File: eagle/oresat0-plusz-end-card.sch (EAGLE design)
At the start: 36 parts, among them J1 Harwin M55-7101242R, J10 R107064070_CONTACT, J11 R107064070_CONTACT, J12 R107064070_CONTACT, J13 R107064070_CONTACT, J14 R107064070_CONTACT, J15 R107064070_CONTACT, J16 R107064070_CONTACT, J2 Harwin M55-7101242R, J3 Harwin M55-7101242R, J4 Harwin M55-7101242R, J6 J-SAMTEC-TFM-120-X1-XXX-D-RA, J7 R107064070_CONTACT, J8 R107064070_CONTACT, J9 R107064070_CONTACT, U1 QCN-19D+, U2 QCN-19D+, U3 QCN-19D+

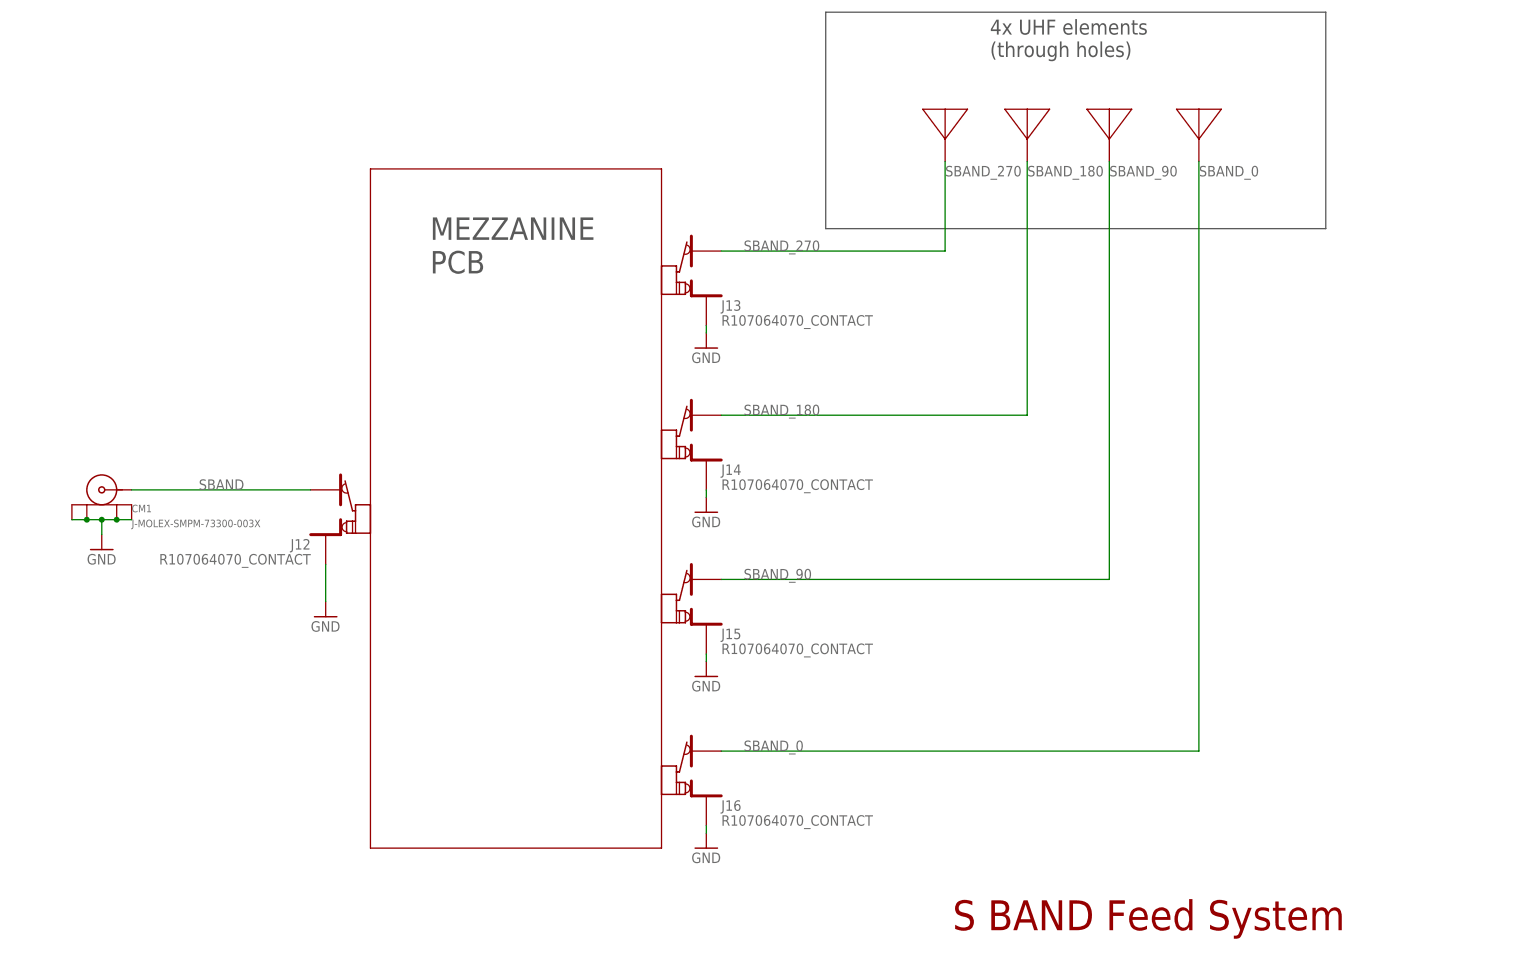
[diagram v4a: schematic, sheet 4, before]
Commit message: Version 1.2 of the OreSat0 end card and mezzanine.
Largest change is the position of the antennas on the end card; changes to the deployer changed the antenna placement which triggered everything else.

Other changes include fiducials, attributes cleanup, move to 0603 resistors, and misc polish.
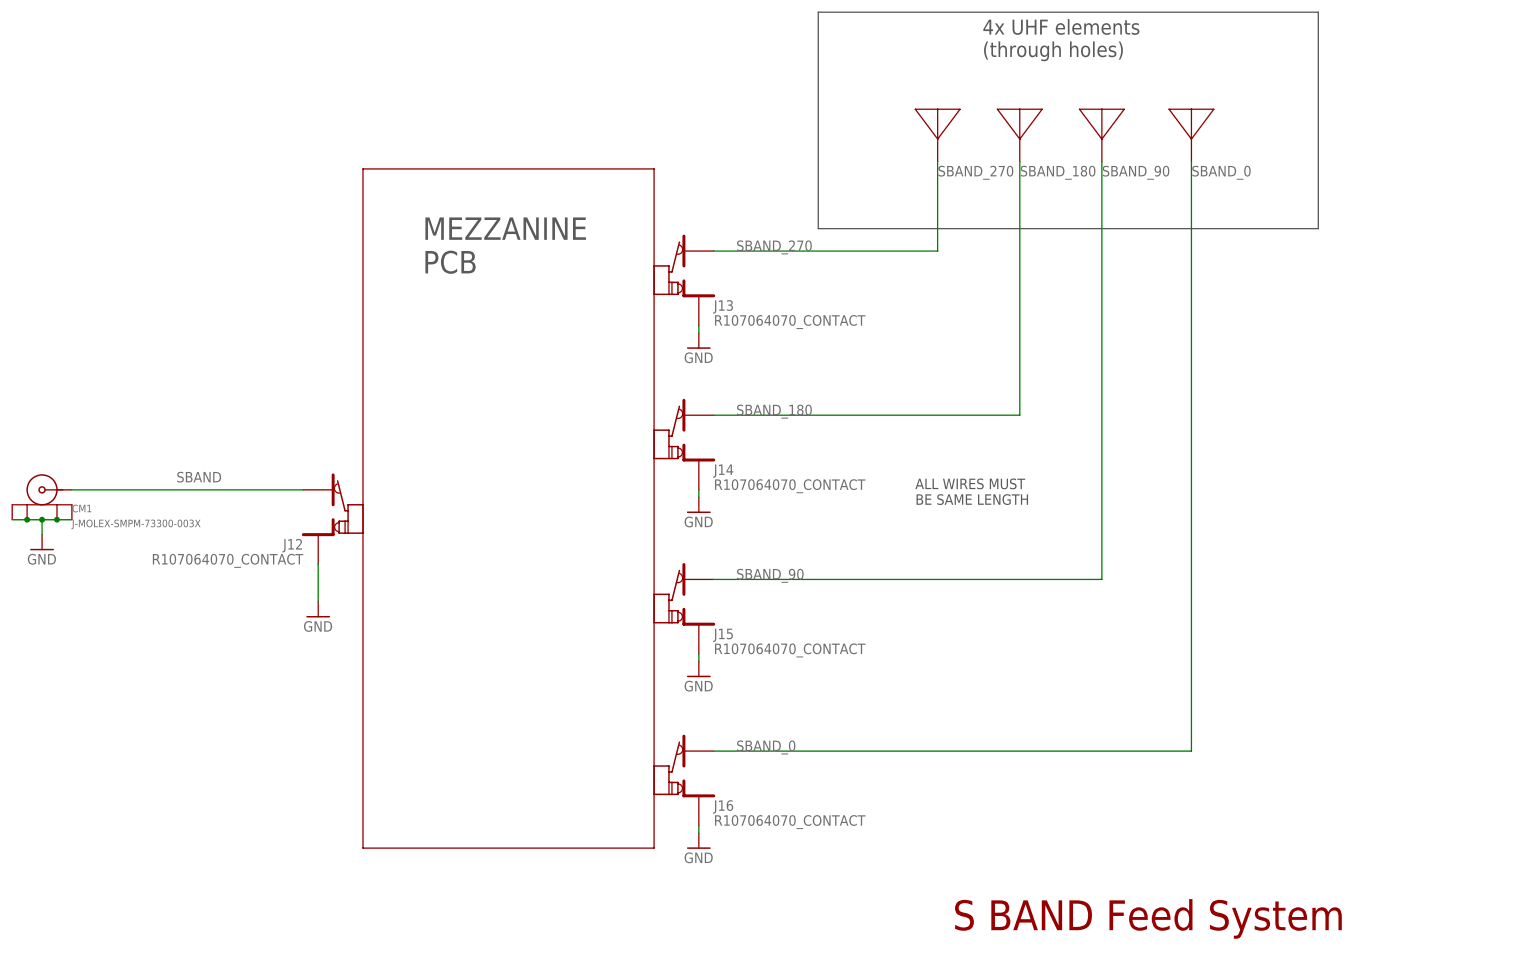
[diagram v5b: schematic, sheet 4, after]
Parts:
- added FIDUCIAL1, FIDUCIAL2, FIDUCIAL3, FIDUCIAL4, FIDUCIAL5, FIDUCIAL6: FIDUCIAL-1.0X2.0, monitor-v2-debug:FIDUCIAL-1.0X2.0
- R1, R2, R3: device oresat-rcl:R-US_0805-B-NOSILK -> oresat-rcl:R-US_0603-C-NOSILK
- R5: value 1 1W -> 7.5 1W; device oresat-rcl:R-US_0309/12 -> R-Vishay-PAC1000-1W-resistor:PAC100-FOR-MELTWIRE
- U1, U2, U3: value QCN-19D+ -> QCN-19+; device Mini-Circuits-QCN-19D+_Phase-shifter:QCN-19D+ -> U-MiniCirc-QCN-XXX+-quad:QCN-XXX+
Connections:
- net LBAND-1/4L: now also U1.PORT2, U3.SUM; no longer U1.90, U2.SUM
- net LBAND-SHORT: now also U1.PORT1, U2.SUM; no longer U1.0, U3.SUM
- net LBAND_0: now also U2.PORT1; no longer U3.0
- net LBAND_180: now also U3.PORT1; no longer U2.0
- net LBAND_270: now also U3.PORT2; no longer U2.90
- net LBAND_90: now also U2.PORT2; no longer U3.90
- net N$4: now also U2.TERM; no longer U3.TERM
- net N$6: now also U3.TERM; no longer U2.TERM
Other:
- note added: "1.2"
- note added: "ALL WIRES MUST BE SAME LENGTH"
- note added: "Fiducials on front and back"
- note added: "Length + 1/4L (+ 36.1 mm )"
- note added: "Meltwire Resistor"
- note added: "PAC100007508FA1000"
- note removed: "1"
- note removed: "36.1 mm on 4 lyr OSH Park PCB"
- note removed: "Meltwire Resistors"
- note removed: "PAC100001008FA1000"
- moved on the sheet: CM1, CM2, CM3, J12, J13, J14, J15, J16, R1

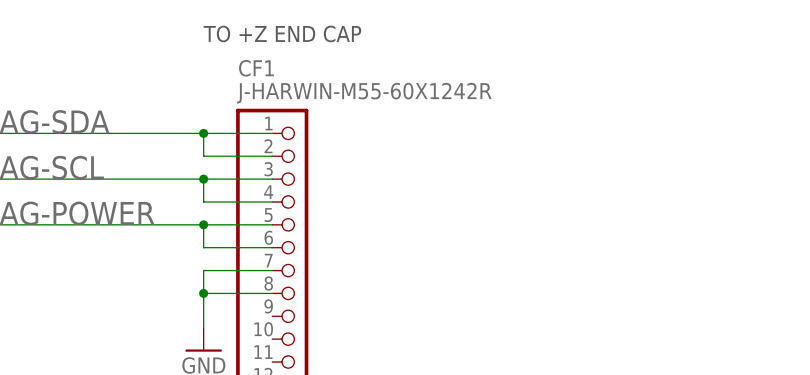
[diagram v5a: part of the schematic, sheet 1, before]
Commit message: Fixed bad part number for end card to end cap connector.
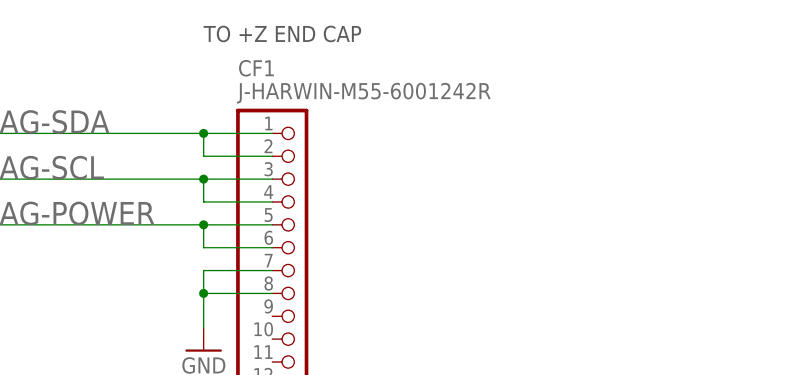
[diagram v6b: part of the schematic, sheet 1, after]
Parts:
- CF1: value J-HARWIN-M55-60X1242R -> J-HARWIN-M55-6001242R
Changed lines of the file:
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@@
 <part name="GND19" library="supply1" library_urn="urn:adsk.eagle:library:371" deviceset="GND" device=""/>
 <part name="GND20" library="supply1" library_urn="urn:adsk.eagle:library:371" deviceset="GND" device=""/>
-<part name="CF1" library="J-Harwin-M55-60X1242R-12pin-1.27mm-F-vertical" deviceset="J-HARWIN-M55-60X1242R" device=""/>
+<part name="CF1" library="J-Harwin-M55-60X1242R-12pin-1.27mm-F-vertical" deviceset="J-HARWIN-M55-60X1242R" device="" value="J-HARWIN-M55-6001242R"/>
 <part name="GND21" library="supply1" library_urn="urn:adsk.eagle:library:371" deviceset="GND" device=""/>
 <part name="GND22" library="supply1" library_urn="urn:adsk.eagle:library:371" deviceset="GND" device=""/>

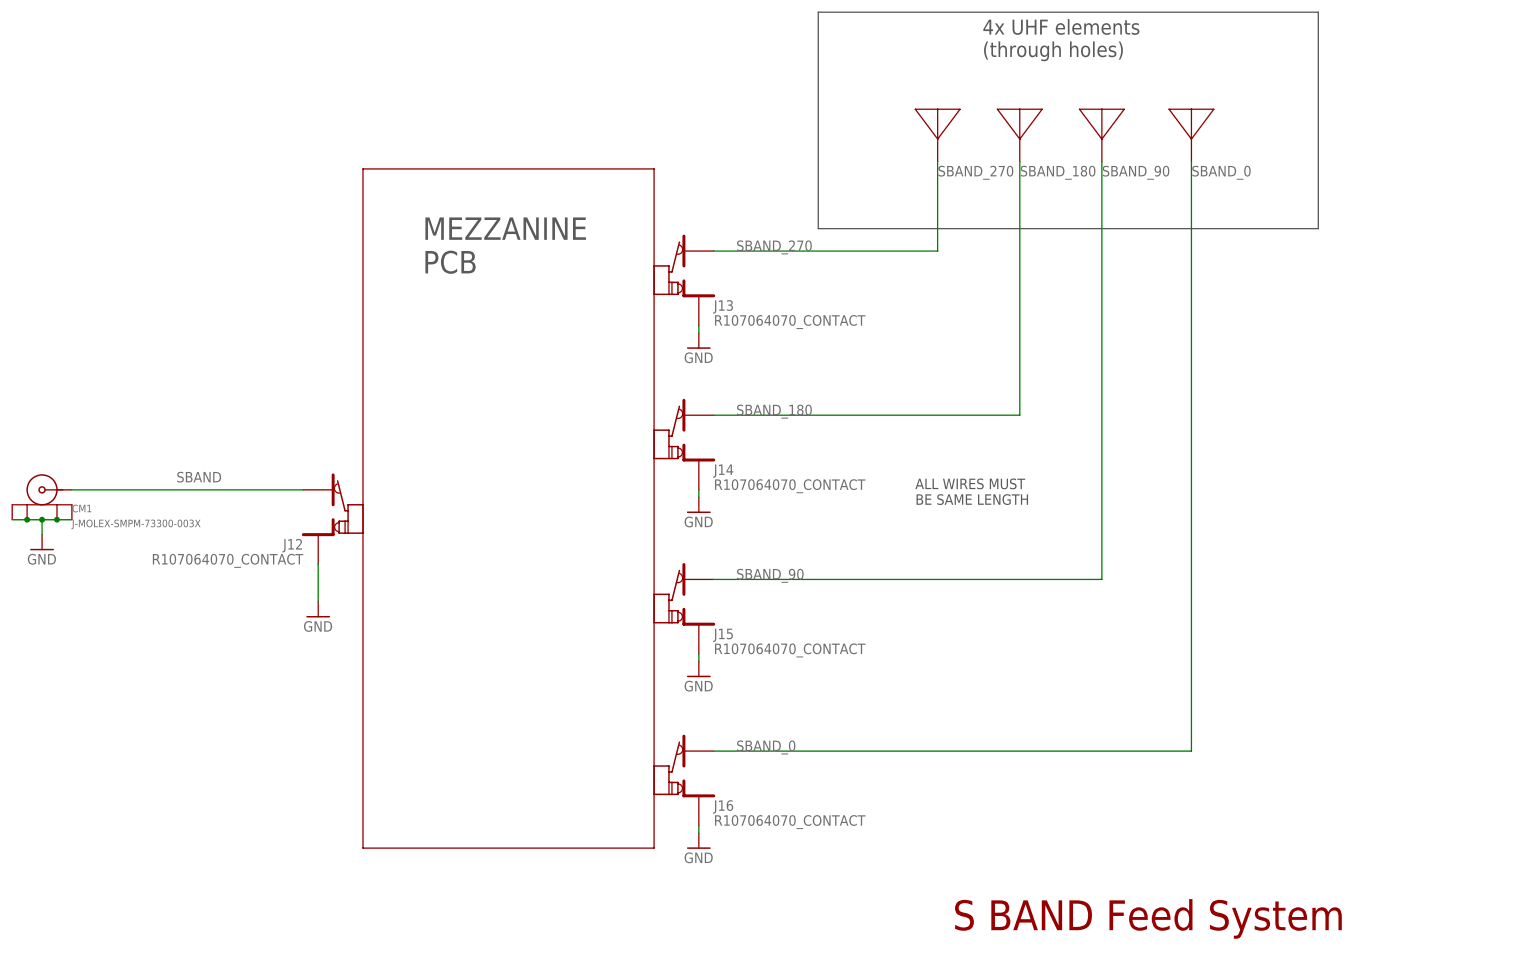
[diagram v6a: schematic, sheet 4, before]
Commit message: replaced S-band net labels with L1-band labels, swapped the S-band hybrids with L-band hybrids, recalculated 1/4 wavelength trace length, routed a new short+1/4 wavelength trace
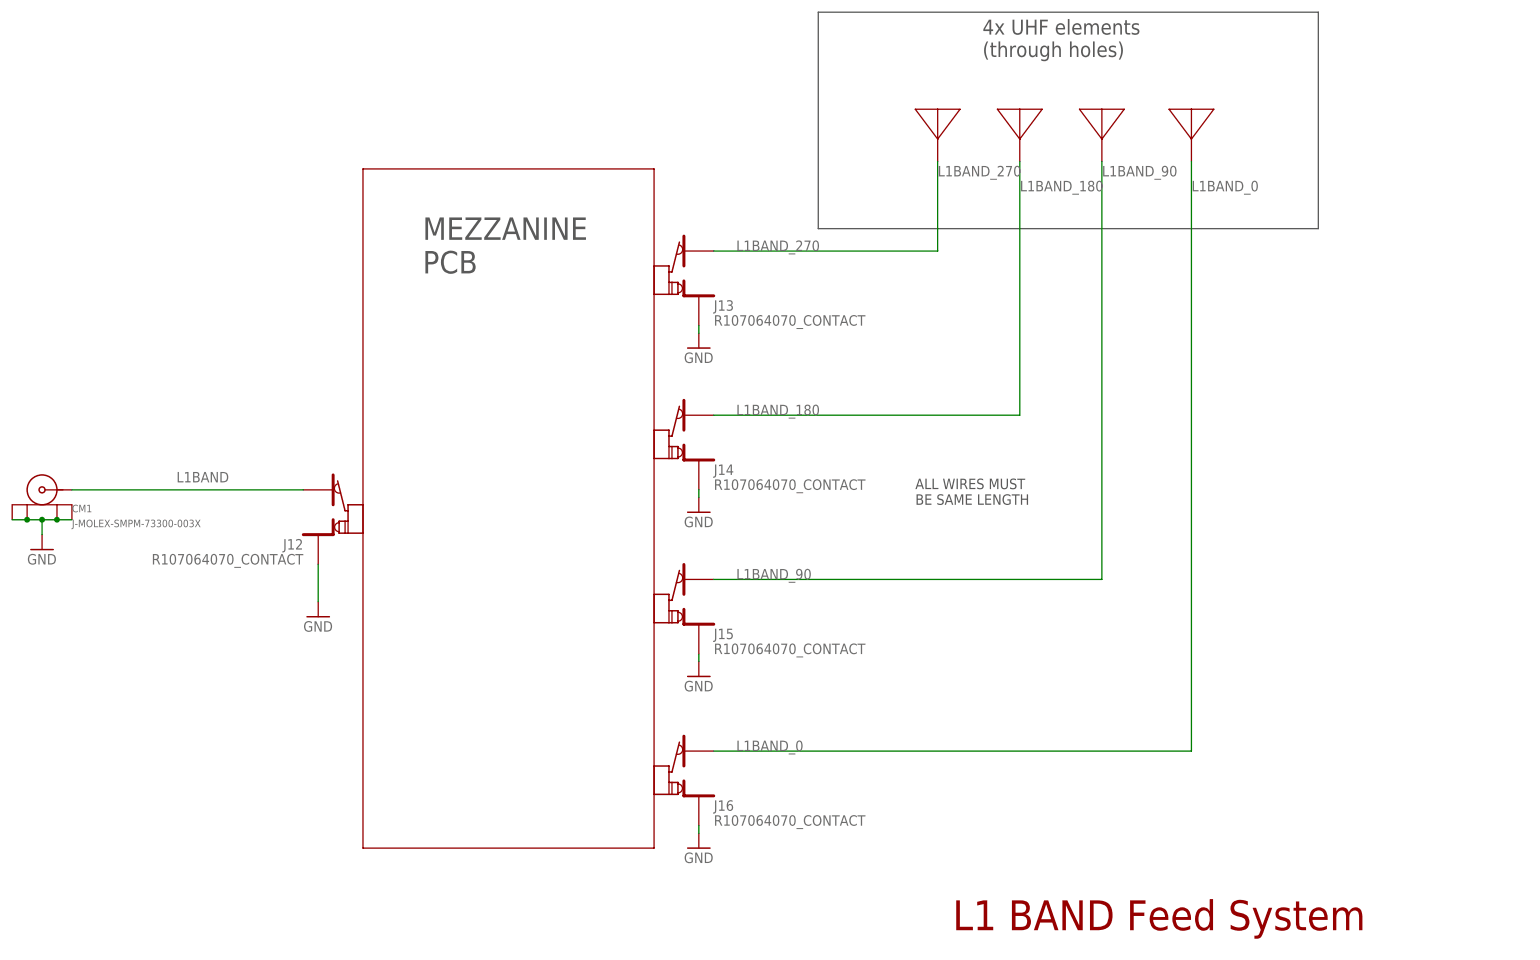
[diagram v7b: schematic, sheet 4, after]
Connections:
- net SBAND renamed L1BAND
- net SBAND_0 renamed L1BAND_0
- net SBAND_180 renamed L1BAND_180
- net SBAND_270 renamed L1BAND_270
- net SBAND_90 renamed L1BAND_90
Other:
- note added: "L1 BAND Feed System"
- note removed: "S BAND Feed System"
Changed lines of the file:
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@@
 <wire x1="238.76" y1="166.37" x2="234.95" y2="161.29" width="0.1524" layer="94"/>
 <wire x1="234.95" y1="161.29" x2="234.95" y2="166.37" width="0.1524" layer="94"/>
-<text x="194.31" y="26.67" size="5.08" layer="94">S BAND Feed System</text>
+<text x="194.31" y="26.67" size="5.08" layer="94">L1 BAND Feed System</text>
 <wire x1="171.45" y1="182.88" x2="171.45" y2="146.05" width="0.1524" layer="97"/>
 <wire x1="171.45" y1="146.05" x2="256.54" y2="146.05" width="0.1524" layer="97"/>
@@
 </segment>
 </net>
-<net name="SBAND_270" class="1">
+<net name="L1BAND_270" class="1">
 <segment>
 <label x="191.77" y="154.94" size="1.778" layer="95"/>
@@
 </segment>
 </net>
-<net name="SBAND_180" class="1">
+<net name="L1BAND_180" class="1">
 <segment>
-<label x="205.74" y="154.94" size="1.778" layer="95"/>
+<label x="205.74" y="152.4" size="1.778" layer="95"/>
 <wire x1="153.67" y1="114.3" x2="205.74" y2="114.3" width="0.1524" layer="91"/>
 <wire x1="205.74" y1="114.3" x2="205.74" y2="157.48" width="0.1524" layer="91"/>
@@
 </segment>
 </net>
-<net name="SBAND_90" class="1">
+<net name="L1BAND_90" class="1">
 <segment>
 <label x="219.71" y="154.94" size="1.778" layer="95"/>
@@
 </segment>
 </net>
-<net name="SBAND_0" class="1">
+<net name="L1BAND_0" class="1">
 <segment>
-<label x="234.95" y="154.94" size="1.778" layer="95"/>
+<label x="234.95" y="152.4" size="1.778" layer="95"/>
 <wire x1="153.67" y1="57.15" x2="234.95" y2="57.15" width="0.1524" layer="91"/>
 <wire x1="234.95" y1="57.15" x2="234.95" y2="157.48" width="0.1524" layer="91"/>
@@
 </segment>
 </net>
-<net name="SBAND" class="1">
+<net name="L1BAND" class="1">
 <segment>
 <pinref part="CM1" gate="G$1" pin="CENTER"/>
